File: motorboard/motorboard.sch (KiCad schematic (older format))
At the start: 9 parts

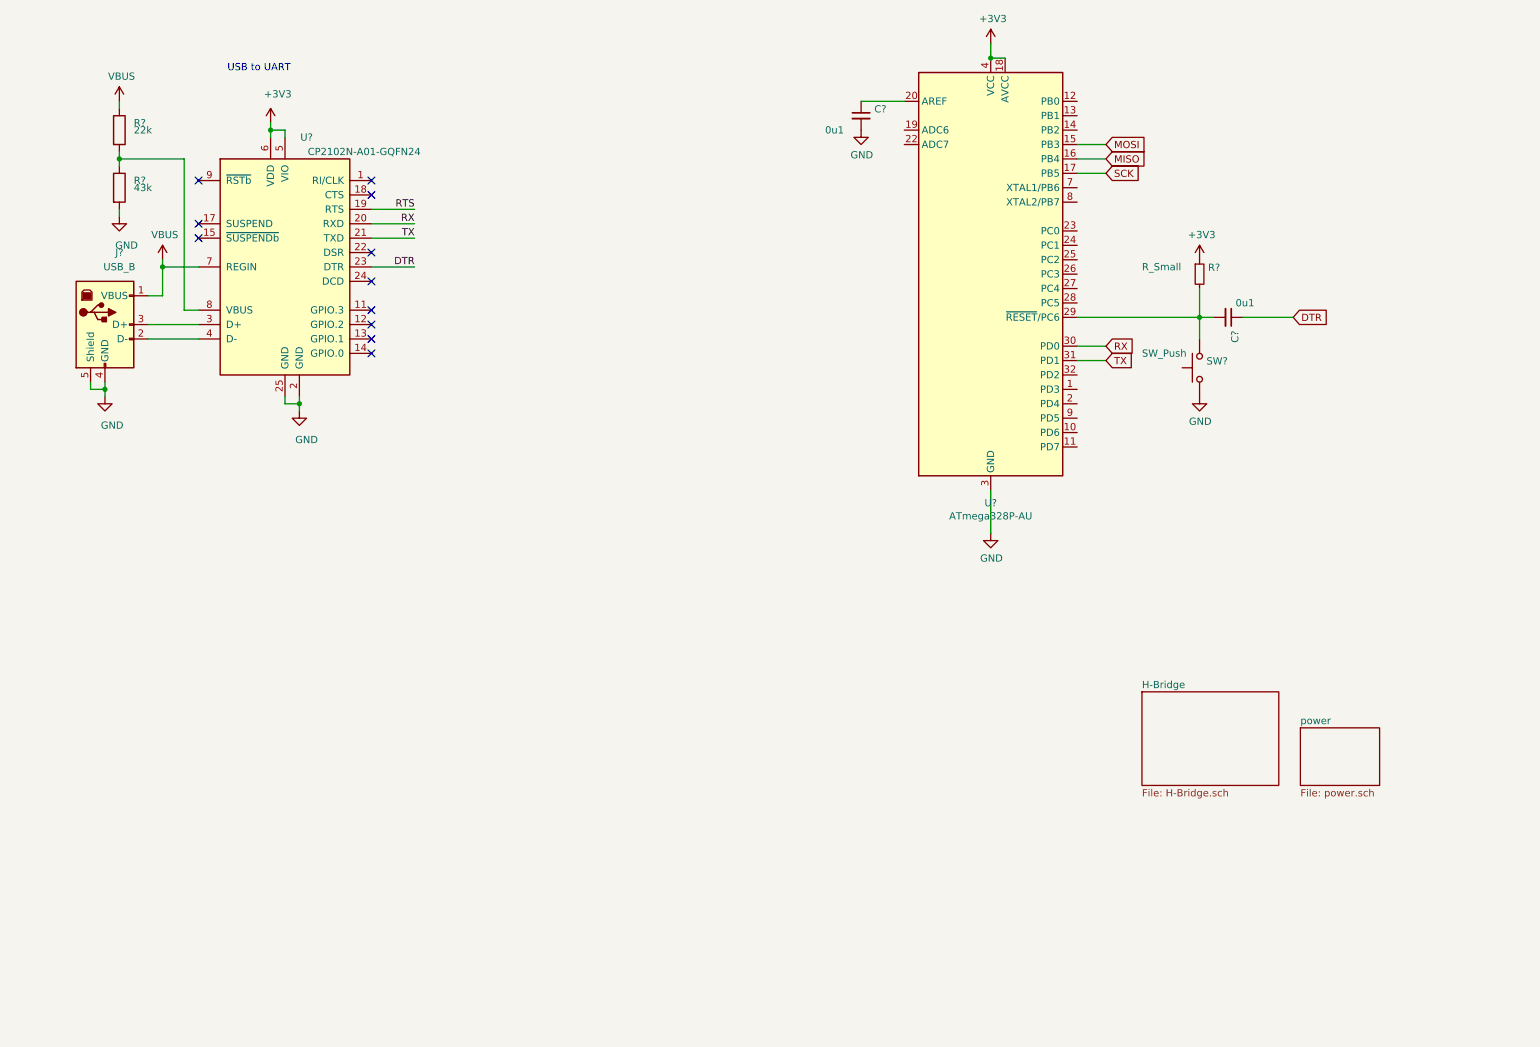
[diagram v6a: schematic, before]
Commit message: H-bridge setup complete
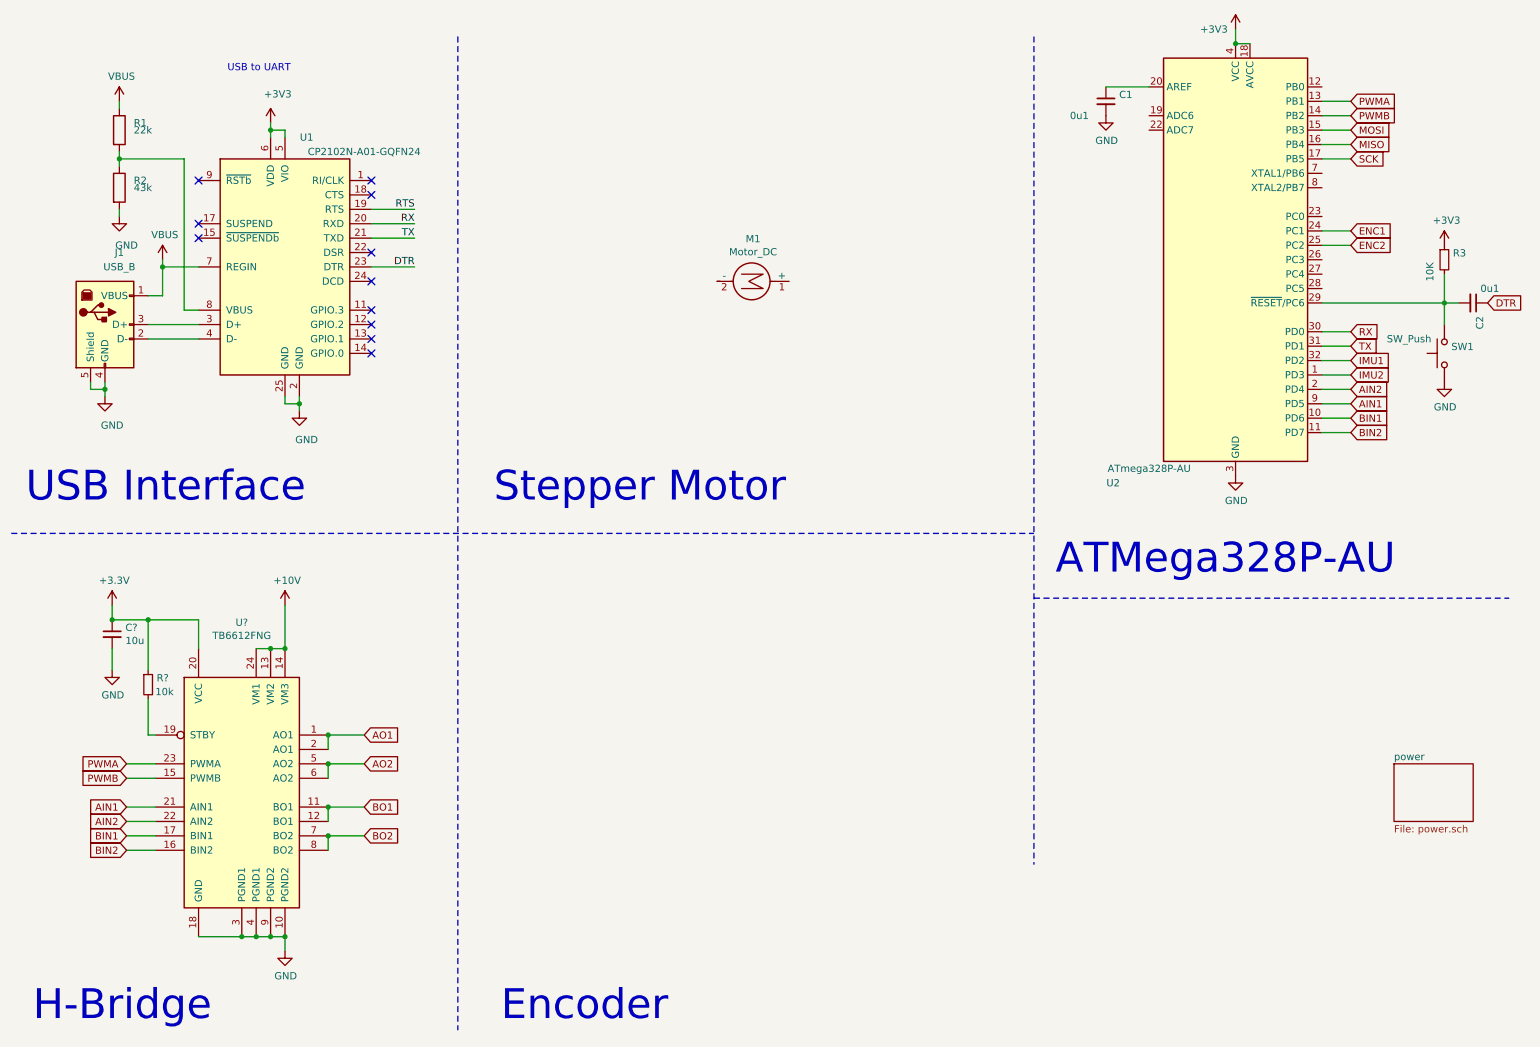
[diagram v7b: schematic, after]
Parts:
- added C?: 10u, symbol Device:C_Small
- added M1: Motor_DC, Connector_PinSocket_2.00mm:PinSocket_1x01_P2.00mm_Vertical, symbol Motor:Motor_DC
- added R?: 10k, symbol Device:R_Small
- added U?: TB6612FNG, Package_SO:SSOP-24_5.3x8.2mm_P0.65mm, symbol Driver_Motor:TB6612FNG
- R3: renamed from R?; value R_Small -> 10K
- gave numbers to parts that had none: 8
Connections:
- net +3V3: now also C?.1, R?.1, U?.20 (VCC)
- net GND: now also C?.2, U?.10 (PGND2), U?.18 (GND), U?.3 (PGND1), U?.4 (PGND1), U?.9 (PGND2)
- net IMU2: now reaches U2.1 (PD3)
- net BIN1: now reaches U2.10 (PD6)
- net BIN1: now also U?.17 (BIN1)
- net BIN2: now reaches U2.11 (PD7)
- net BIN2: now also U?.16 (BIN2)
- net PWMA: now reaches U2.13 (PB1)
- net PWMA: now also U?.23 (PWMA)
- net PWMB: now reaches U2.14 (PB2)
- net PWMB: now also U?.15 (PWMB)
- net AIN2: now reaches U2.2 (PD4)
- net AIN2: now also U?.22 (AIN2)
- net ENC1: now reaches U2.24 (PC1)
- net ENC2: now reaches U2.25 (PC2)
- net IMU1: now reaches U2.32 (PD2)
- net AIN1: now reaches U2.9 (PD5)
- net AIN1: now also U?.21 (AIN1)
- new net: R?.2, U?.19 (STBY)
- new net +10V: U?.13 (VM2), U?.14 (VM3), U?.24 (VM1)
- new net AO1: U?.1 (AO1), U?.2 (AO1)
- new net AO2: U?.5 (AO2), U?.6 (AO2)
- new net BO1: U?.11 (BO1), U?.12 (BO1)
- new net BO2: U?.7 (BO2), U?.8 (BO2)
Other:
- note added: "ATMega328P-AU"
- note added: "Encoder"
- note added: "H-Bridge"
- note added: "Stepper Motor"
- note added: "USB Interface"
- moved on the sheet: C1, C2, R3, SW1, U2

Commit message: Encoder started
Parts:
- removed M1: Motor_DC, Connector_PinSocket_2.00mm:PinSocket_1x01_P2.00mm_Vertical, symbol Motor:Motor_DC
- added C?: 100n, symbol Device:C_Small
- added J?: Conn_01x04_Male, Connector_PinSocket_2.00mm:PinSocket_1x04_P2.00mm_Vertical, symbol Connector:Conn_01x04_Male
- added U?: AS5600-ASOM, SOIC127P600X175-8N, symbol AS5600:AS5600-ASOM
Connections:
- net +3V3: now also C?.1, U?.1 (VDD5V), U?.2 (VDD3V3)
- net AO1: now also J?.1 (Pin_1)
- net AO2: now also J?.2 (Pin_2)
- net BO1: now also J?.3 (Pin_3)
- net BO2: now also J?.4 (Pin_4)
- net GND: now also C?.2, U?.4 (GND)
- net ENC: now reaches U2.26 (PC3)
- net ENC: now also U?.3 (OUT)
- net SCL: now reaches U2.27 (PC4)
- net SDA: now reaches U2.28 (PC5)
- net ENC1: no longer names the net of U2.24 (PC1)
- net ENC2: no longer names the net of U2.25 (PC2)
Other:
- note added: "Blue"
- note added: "MOTORBOARD"
- note added: "Red"
- note added: "THE INCREDIBLE"
- note added: "White"
- note added: "Yellow"
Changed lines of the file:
@@
 $EndDescr
 $Sheet
-S 10300 5750 550  400
+S 9300 5400 550  400
 U 5DAD2180
 F0 "power" 50
@@
 	1    9200 2250
 	1    0    0    -1
-$EndComp
-$Comp
-L Motor:Motor_DC M?
-U 1 1 5E38606B
-P 5900 2400
-AR Path="/5E41532A/5E38606B" Ref="M?"  Part="1"
-AR Path="/5E38606B" Ref="M1"  Part="1"
-F 0 "M1" V 5605 2350 50  0000 C CNN
-F 1 "Motor_DC" V 5696 2350 50  0000 C CNN
-F 2 "Connector_PinSocket_2.00mm:PinSocket_1x01_P2.00mm_Vertical" H 5900 2310 50  0001 C CNN
-F 3 "~" H 5900 2310 50  0001 C CNN
-	1    5900 2400
-	0    1    1    0
 $EndComp
 Wire Wire Line
@@
 Text Notes 850  7550 0    207  ~ 0
 H-Bridge
-Wire Notes Line
-	3800 700  3800 7600
 Text Notes 800  3950 0    207  ~ 0
 USB Interface
-Wire Wire Line
-	9800 2050 10000 2050
-Wire Wire Line
-	9800 2150 10000 2150
 Wire Wire Line
 	9800 2950 10000 2950
@@
 Text GLabel 10000 3050 2    50   Input ~ 0
 IMU2
-Text GLabel 10000 2050 2    50   Input ~ 0
-ENC1
-Text GLabel 10000 2150 2    50   Input ~ 0
-ENC2
 Text Notes 7950 4450 0    207  ~ 0
 ATMega328P-AU
 Wire Notes Line
 	7800 4600 11100 4600
+Text Notes 4050 2900 0    207  ~ 0
+Stepper Motor
+Text Notes 4100 7550 0    207  ~ 0
+Encoder
 Wire Notes Line
-	700  4150 7800 4150
-Text Notes 4050 3950 0    207  ~ 0
-Stepper Motor
+	3800 1600 7800 1600
+Text Notes 4400 1400 0    286  ~ 57
+MOTORBOARD
+Text Notes 5000 900  0    128  ~ 26
+THE INCREDIBLE
+$Comp
+L AS5600:AS5600-ASOM U?
+U 1 1 5E3DA57E
+P 5750 5100
+F 0 "U?" H 5750 5970 50  0000 C CNN
+F 1 "AS5600-ASOM" H 5750 5879 50  0000 C CNN
+F 2 "SOIC127P600X175-8N" H 5750 5100 50  0001 L BNN
+F 3 "ams" H 5750 5100 50  0001 L BNN
+F 4 "SOIC127P600X175-8N" H 5750 5100 50  0001 L BNN "Field4"
+	1    5750 5100
+	1    0    0    -1
+$EndComp
+$Comp
+L Connector:Conn_01x04_Male J?
+U 1 1 5E3DBB95
+P 5600 2100
+F 0 "J?" H 5708 2381 50  0000 C CNN
+F 1 "Conn_01x04_Male" H 5708 2290 50  0000 C CNN
+F 2 "Connector_PinSocket_2.00mm:PinSocket_1x04_P2.00mm_Vertical" H 5600 2100 50  0001 C CNN
+F 3 "~" H 5600 2100 50  0001 C CNN
+	1    5600 2100
+	1    0    0    -1
+$EndComp
+Wire Wire Line
+	5800 2000 6000 2000
+Wire Wire Line
+	5800 2100 6000 2100
+Wire Wire Line
+	5800 2200 6000 2200
+Wire Wire Line
+	5800 2300 6000 2300
+Text GLabel 6000 2000 2    50   Input ~ 0
+AO1
+Text GLabel 6000 2100 2    50   Input ~ 0
+AO2
+Text GLabel 6000 2200 2    50   Input ~ 0
+BO1
+Text GLabel 6000 2300 2    50   Input ~ 0
+BO2
+Wire Notes Line
+	3800 4100 750  4100
+Wire Notes Line
+	3800 700  3800 7600
+Wire Notes Line
+	3800 3150 7800 3150
 Wire Notes Line
 	7800 700  7800 6450
-Text Notes 4100 7550 0    207  ~ 0
-Encoder
+Text Notes 6250 2050 0    50   ~ 0
+White
+Text Notes 6250 2150 0    50   ~ 0
+Blue
+Text Notes 6250 2250 0    50   ~ 0
+Red
+Text Notes 6250 2350 0    50   ~ 0
+Yellow
+Wire Wire Line
+	9800 2350 10000 2350
+Wire Wire Line
+	9800 2450 10000 2450
+Text GLabel 10000 2350 2    50   Input ~ 0
+SCL
+Text GLabel 10000 2450 2    50   Input ~ 0
+SDA
+Wire Wire Line
+	5050 4800 4850 4800
+Wire Wire Line
+	5050 5000 4850 5000
+Wire Wire Line
+	5050 5400 4850 5400
+Wire Wire Line
+	6450 5600 6450 5750
+Wire Wire Line
+	9800 2250 10000 2250
+Text GLabel 10000 2250 2    50   Input ~ 0
+ENC
+Wire Wire Line
+	6450 4800 6650 4800
+Text GLabel 6650 4800 2    50   Input ~ 0
+ENC
+$Comp
+L power:+3V3 #PWR?
+U 1 1 5E41B8C5
+P 6450 4350
+F 0 "#PWR?" H 6450 4200 50  0001 C CNN
+F 1 "+3V3" H 6465 4523 50  0000 C CNN
+F 2 "" H 6450 4350 50  0001 C CNN
+F 3 "" H 6450 4350 50  0001 C CNN
+	1    6450 4350
+	1    0    0    -1
+$EndComp
+$Comp
+L power:GND #PWR?
+U 1 1 5E41C064
+P 6450 5750
+F 0 "#PWR?" H 6450 5500 50  0001 C CNN
+F 1 "GND" H 6455 5577 50  0000 C CNN
+F 2 "" H 6450 5750 50  0001 C CNN
+F 3 "" H 6450 5750 50  0001 C CNN
+	1    6450 5750
+	1    0    0    -1
+$EndComp
+Wire Wire Line
+	6450 4600 6450 4500
+Wire Wire Line
+	6450 4500 6650 4500
+Connection ~ 6450 4500
+$Comp
+L Device:C_Small C?
+U 1 1 5E421ADD
+P 6750 4500
+F 0 "C?" V 6979 4500 50  0000 C CNN
+F 1 "100n" V 6888 4500 50  0000 C CNN
+F 2 "" H 6750 4500 50  0001 C CNN
+F 3 "~" H 6750 4500 50  0001 C CNN
+	1    6750 4500
+	0    -1   -1   0
+$EndComp
+$Comp
+L power:GND #PWR?
+U 1 1 5E422555
+P 7000 4550
+F 0 "#PWR?" H 7000 4300 50  0001 C CNN
+F 1 "GND" H 7005 4377 50  0000 C CNN
+F 2 "" H 7000 4550 50  0001 C CNN
+F 3 "" H 7000 4550 50  0001 C CNN
+	1    7000 4550
+	1    0    0    -1
+$EndComp
+Wire Wire Line
+	6850 4500 7000 4500
+Wire Wire Line
+	7000 4500 7000 4550
+Wire Wire Line
+	6450 4500 6450 4350
 $EndSCHEMATC
